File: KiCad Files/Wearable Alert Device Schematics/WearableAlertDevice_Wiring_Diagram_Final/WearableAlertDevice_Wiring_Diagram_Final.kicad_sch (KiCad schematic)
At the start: 8 parts

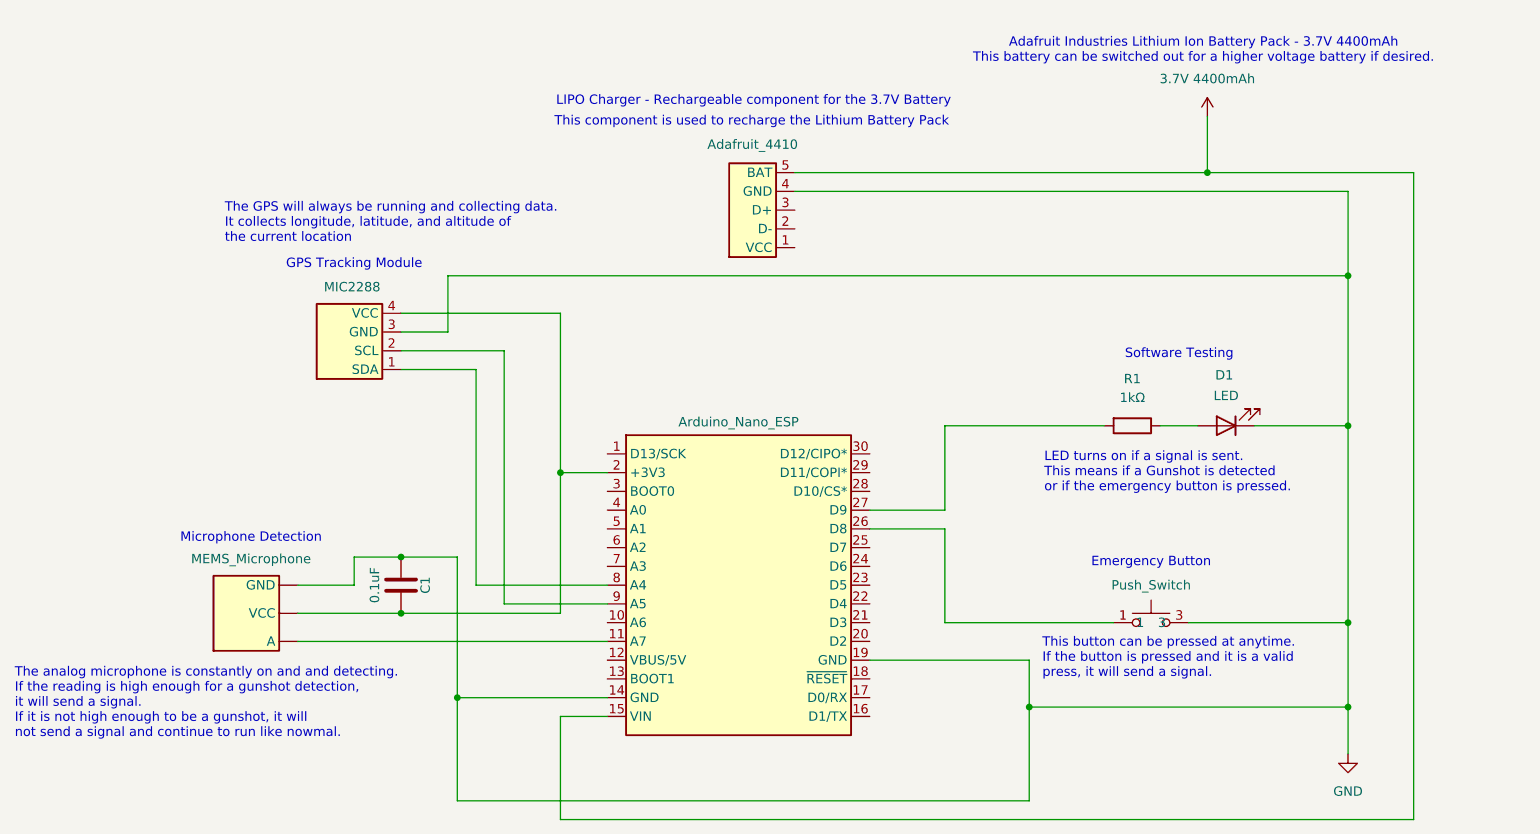
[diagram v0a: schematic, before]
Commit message: Change Symbol for Lipo Charger
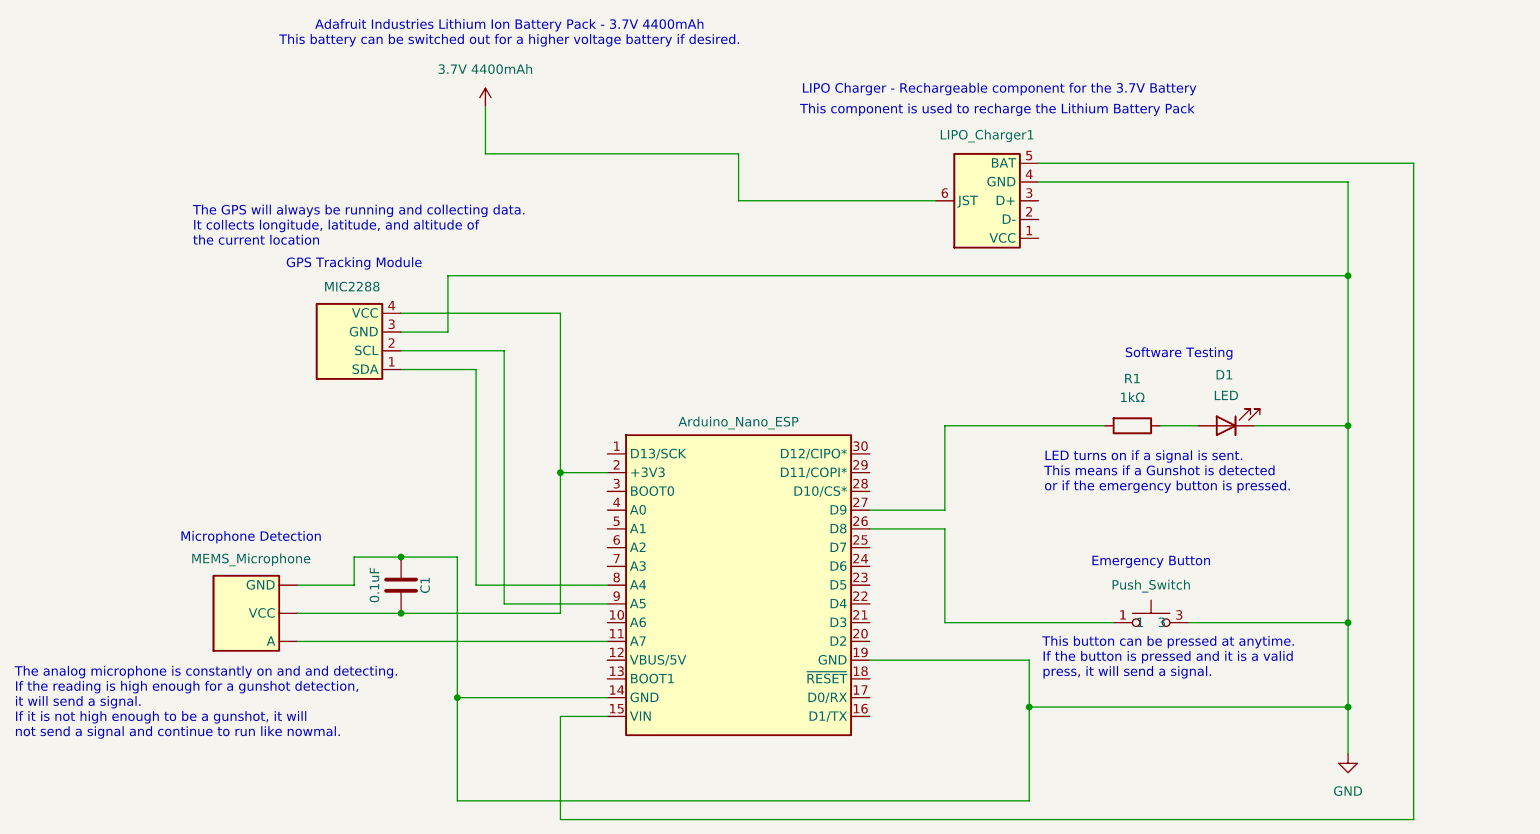
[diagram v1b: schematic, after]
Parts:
- removed Adafruit_4410: (no value), symbol CCEW Wearable Alert Library:LIPO_Charger
- added LIPO_Charger1: (no value), symbol CCEW Wearable Alert Library:LIPO_Charger
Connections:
- net 3.7V 4400mAh: now also LIPO_Charger1.6 (JST); no longer Arduino_Nano_ESP.15 (VIN)
- net GND: now also LIPO_Charger1.4 (GND)
- new net: Arduino_Nano_ESP.15 (VIN), LIPO_Charger1.5 (BAT)
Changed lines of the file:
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@@
 	(text "The GPS will always be running and collecting data.\nIt collects longitude, latitude, and altitude of\nthe current location"
 		(exclude_from_sim no)
-		(at 70.104 65.278 0)
+		(at 65.786 65.786 0)
 		(effects
 			(font
@@
 	(text "Adafruit Industries Lithium Ion Battery Pack - 3.7V 4400mAh\nThis battery can be switched out for a higher voltage battery if desired."
 		(exclude_from_sim no)
-		(at 202.692 41.91 0)
+		(at 108.712 39.624 0)
 		(effects
 			(font
@@
 	(text "LIPO Charger - Rechargeable component for the 3.7V Battery"
 		(exclude_from_sim no)
-		(at 141.732 48.768 0)
+		(at 175.006 47.244 0)
 		(effects
 			(font
@@
 	(text "This component is used to recharge the Lithium Battery Pack"
 		(exclude_from_sim no)
-		(at 141.478 51.562 0)
+		(at 174.752 50.038 0)
 		(effects
 			(font
@@
 	)
 	(junction
-		(at 203.2 58.42)
-		(diameter 0)
-		(color 0 0 0 0)
-	)
-	(junction
 		(at 222.25 72.39)
 		(diameter 0)
@@
 	(wire
 		(pts
-			(xy 203.2 58.42) (xy 231.14 58.42)
-		)
-		(stroke
-			(width 0)
-			(type default)
-		)
-	)
-	(wire
-		(pts
 			(xy 100.33 80.01) (xy 100.33 72.39)
 		)
@@
 	(wire
 		(pts
+			(xy 105.41 49.53) (xy 105.41 55.88)
+		)
+		(stroke
+			(width 0)
+			(type default)
+		)
+	)
+	(wire
+		(pts
 			(xy 200.66 119.38) (xy 222.25 119.38)
 		)
@@
 	(wire
 		(pts
-			(xy 231.14 58.42) (xy 231.14 146.05)
+			(xy 105.41 55.88) (xy 139.7 55.88)
+		)
+		(stroke
+			(width 0)
+			(type default)
+		)
+	)
+	(wire
+		(pts
+			(xy 231.14 57.15) (xy 231.14 146.05)
 		)
 		(stroke
@@
 	(wire
 		(pts
-			(xy 203.2 50.8) (xy 203.2 58.42)
-		)
-		(stroke
-			(width 0)
-			(type default)
-		)
-	)
-	(wire
-		(pts
 			(xy 80.01 118.11) (xy 93.98 118.11)
 		)
@@
 	(wire
 		(pts
-			(xy 222.25 60.96) (xy 222.25 72.39)
+			(xy 222.25 59.69) (xy 222.25 72.39)
 		)
 		(stroke
@@
 	(wire
 		(pts
-			(xy 147.32 60.96) (xy 222.25 60.96)
+			(xy 180.34 59.69) (xy 222.25 59.69)
 		)
 		(stroke
@@
 	(wire
 		(pts
-			(xy 147.32 58.42) (xy 203.2 58.42)
+			(xy 139.7 62.23) (xy 166.37 62.23)
+		)
+		(stroke
+			(width 0)
+			(type default)
+		)
+	)
+	(wire
+		(pts
+			(xy 180.34 57.15) (xy 231.14 57.15)
 		)
 		(stroke
@@
 	(wire
 		(pts
+			(xy 139.7 55.88) (xy 139.7 62.23)
+		)
+		(stroke
+			(width 0)
+			(type default)
+		)
+	)
+	(wire
+		(pts
 			(xy 179.07 143.51) (xy 179.07 130.81)
 		)
@@
 			(width 0)
 			(type default)
-		)
-	)
-	(symbol
-		(lib_id "CCEW Wearable Alert Library:LIPO_Charger")
-		(at 144.78 69.85 90)
-		(unit 1)
-		(body_style 1)
-		(exclude_from_sim no)
-		(in_bom yes)
-		(on_board yes)
-		(in_pos_files yes)
-		(dnp no)
-		(fields_autoplaced yes)
-		(property "Reference" "Adafruit_4410"
-			(at 141.605 54.61 90)
-			(show_name no)
-			(do_not_autoplace no)
-			(effects
-				(font
-					(size 1.27 1.27)
-				)
-			)
-		)
-		(property "Value" ""
-			(at 144.78 69.85 0)
-			(show_name no)
-			(do_not_autoplace no)
-			(effects
-				(font
-					(size 1.27 1.27)
-				)
-			)
-		)
-		(property "Footprint" ""
-			(at 144.78 69.85 0)
-			(hide yes)
-			(show_name no)
-			(do_not_autoplace no)
-			(effects
-				(font
-					(size 1.27 1.27)
-				)
-			)
-		)
-		(property "Datasheet" ""
-			(at 144.78 69.85 0)
-			(hide yes)
-			(show_name no)
-			(do_not_autoplace no)
-			(effects
-				(font
-					(size 1.27 1.27)
-				)
-			)
-		)
-		(property "Description" ""
-			(at 144.78 69.85 0)
-			(hide yes)
-			(show_name no)
-			(do_not_autoplace no)
-			(effects
-				(font
-					(size 1.27 1.27)
-				)
-			)
-		)
-		(pin "4"
-		)
-		(pin "5"
-		)
-		(pin "3"
-		)
-		(pin "1"
-		)
-		(pin "2"
-		)
-		(instances
-			(project "WearableAlertDevice_Wiring_Diagram_Final"
-				(path "/ab575065-7949-4984-bd74-060dfe22f1fc"
-					(reference "Adafruit_4410")
-					(unit 1)
-				)
-			)
 		)
 	)
@@
 	(symbol
 		(lib_id "power:VCC")
-		(at 203.2 50.8 0)
+		(at 105.41 49.53 0)
 		(unit 1)
 		(body_style 1)
@@
 		(fields_autoplaced yes)
 		(property "Reference" "#PWR01"
-			(at 203.2 54.61 0)
+			(at 105.41 53.34 0)
 			(hide yes)
 			(show_name no)
@@
 		)
 		(property "Value" "3.7V 4400mAh"
-			(at 203.2 45.72 0)
+			(at 105.41 44.45 0)
 			(show_name no)
 			(do_not_autoplace no)
@@
 		)
 		(property "Footprint" ""
-			(at 203.2 50.8 0)
+			(at 105.41 49.53 0)
 			(hide yes)
 			(show_name no)
@@
 		)
 		(property "Datasheet" ""
-			(at 203.2 50.8 0)
+			(at 105.41 49.53 0)
 			(hide yes)
 			(show_name no)
@@
 		)
 		(property "Description" "Power symbol creates a global label with name \"VCC\""
-			(at 203.2 50.8 0)
+			(at 105.41 49.53 0)
 			(hide yes)
 			(show_name no)
@@
 					(unit 1)
 				)
+			)
+		)
+	)
+	(symbol
+		(lib_id "CCEW Wearable Alert Library:LIPO_Charger")
+		(at 177.8 68.58 90)
+		(unit 1)
+		(body_style 1)
+		(exclude_from_sim no)
+		(in_bom yes)
+		(on_board yes)
+		(in_pos_files yes)
+		(dnp no)
+		(fields_autoplaced yes)
+		(property "Reference" "LIPO_Charger1"
+			(at 173.355 53.34 90)
+			(show_name no)
+			(do_not_autoplace no)
+			(effects
+				(font
+					(size 1.27 1.27)
+				)
+			)
+		)
+		(property "Value" ""
+			(at 177.8 68.58 0)
+			(show_name no)
+			(do_not_autoplace no)
+			(effects
+				(font
+					(size 1.27 1.27)
+				)
+			)
+		)
+		(property "Footprint" ""
+			(at 177.8 68.58 0)
+			(hide yes)
+			(show_name no)
+			(do_not_autoplace no)
+			(effects
+				(font
+					(size 1.27 1.27)
+				)
+			)
+		)
+		(property "Datasheet" ""
+			(at 177.8 68.58 0)
+			(hide yes)
+			(show_name no)
+			(do_not_autoplace no)
+			(effects
+				(font
+					(size 1.27 1.27)
+				)
+			)
+		)
+		(property "Description" "LIPOLY BATTERY CHARGER W/USB C"
+			(at 177.8 68.58 0)
+			(hide yes)
+			(show_name no)
+			(do_not_autoplace no)
+			(effects
+				(font
+					(size 1.27 1.27)
+				)
+			)
+		)
+		(pin "1"
+		)
+		(pin "4"
+		)
+		(pin "2"
+		)
+		(pin "3"
+		)
+		(pin "5"
+		)
+		(pin "6"
+		)
+		(instances
+			(project "WearableAlertDevice_Wiring_Diagram_Final"
+				(path "/ab575065-7949-4984-bd74-060dfe22f1fc"
+					(reference "LIPO_Charger1")
+					(unit 1)
+				)

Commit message: Updated GPS Name
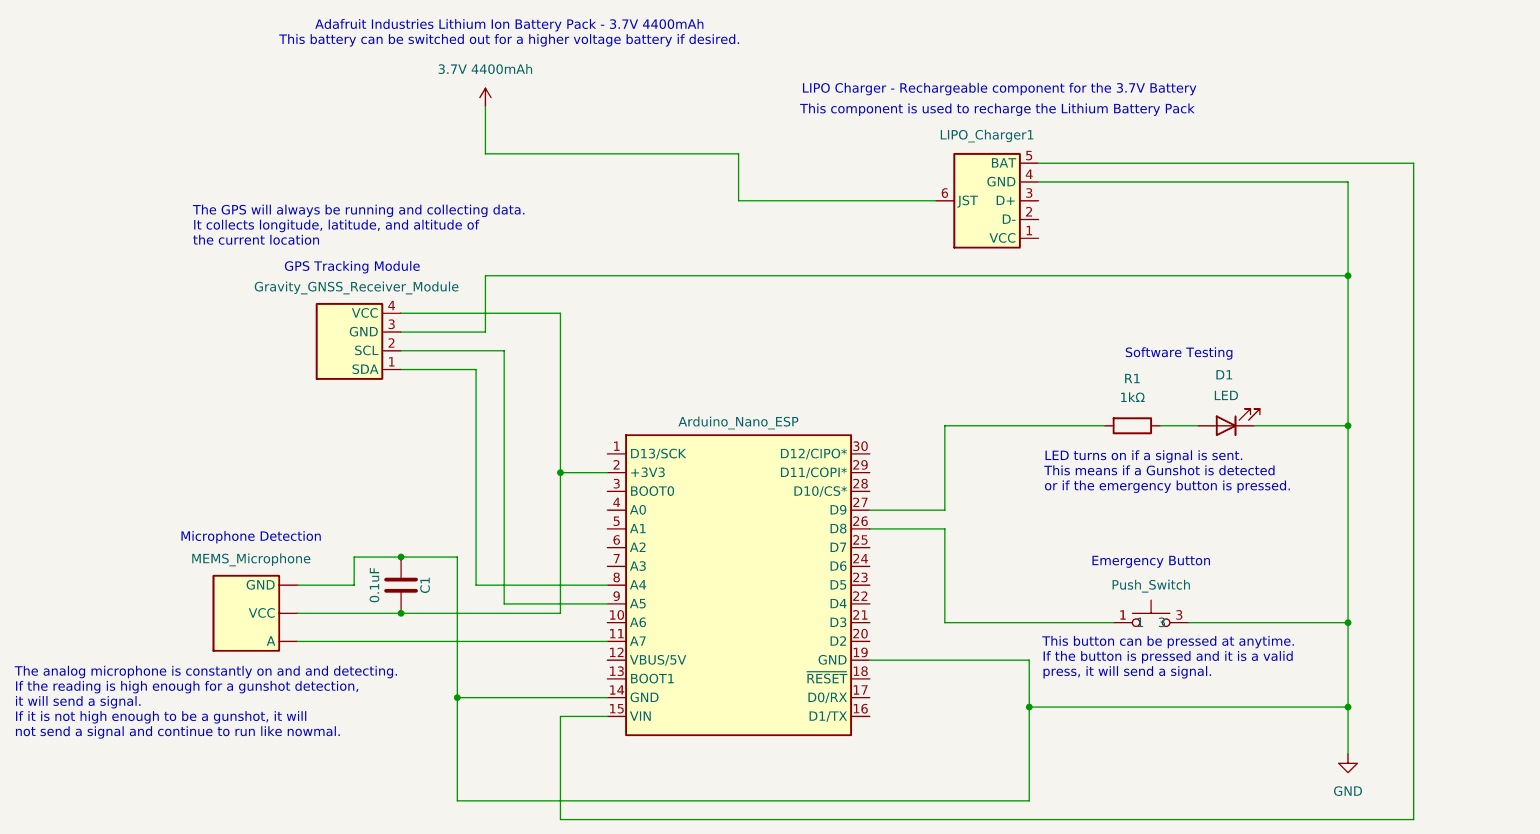
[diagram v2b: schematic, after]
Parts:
- renumbered MIC2288 to Gravity_GNSS_Receiver_Module
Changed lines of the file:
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@@
 	(text "GPS Tracking Module\n"
 		(exclude_from_sim no)
-		(at 87.63 70.866 0)
+		(at 87.376 71.374 0)
 		(effects
 			(font
@@
 	)
 	(junction
+		(at 222.25 72.39)
+		(diameter 0)
+		(color 0 0 0 0)
+	)
+	(junction
 		(at 222.25 130.81)
 		(diameter 0)
@@
 	)
 	(junction
-		(at 222.25 72.39)
-		(diameter 0)
-		(color 0 0 0 0)
-	)
-	(junction
 		(at 115.57 99.06)
 		(diameter 0)
@@
 	(wire
 		(pts
-			(xy 100.33 80.01) (xy 100.33 72.39)
+			(xy 105.41 80.01) (xy 105.41 72.39)
 		)
 		(stroke
@@
 	(wire
 		(pts
-			(xy 93.98 80.01) (xy 100.33 80.01)
+			(xy 93.98 80.01) (xy 105.41 80.01)
 		)
 		(stroke
@@
 	(wire
 		(pts
-			(xy 100.33 72.39) (xy 222.25 72.39)
+			(xy 105.41 72.39) (xy 222.25 72.39)
 		)
 		(stroke
@@
 		(in_pos_files yes)
 		(dnp no)
-		(property "Reference" "MIC2288"
-			(at 91.186 73.914 90)
+		(property "Reference" "Gravity_GNSS_Receiver_Module"
+			(at 101.854 73.914 90)
 			(show_name no)
 			(do_not_autoplace no)
@@
 			(project "WearableAlertDevice_Wiring_Diagram_Final"
 				(path "/ab575065-7949-4984-bd74-060dfe22f1fc"
-					(reference "MIC2288")
+					(reference "Gravity_GNSS_Receiver_Module")
 					(unit 1)
 				)

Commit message: Add Team Names, Date, and Project name
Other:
- company: (none) -> CCEW
- title: (none) -> Wearable Alert Device Wiring Diagram
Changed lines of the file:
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@@
 	(generator_version "10.0")
 	(paper "A4")
+	(title_block
+		(title "Wearable Alert Device Wiring Diagram")
+		(date "2026-05-04")
+		(company "CCEW")
+		(comment 1 "Team Members: Jonas Wollman, Ryan Kiesau, Cody Chan, Alex Ho")
+	)
 	(text "Software Testing"
 		(exclude_from_sim no)
